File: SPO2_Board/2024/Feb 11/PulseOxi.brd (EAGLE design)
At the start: 70 x 70 mm, 45 parts, among them IC1 AFE4400RHAR

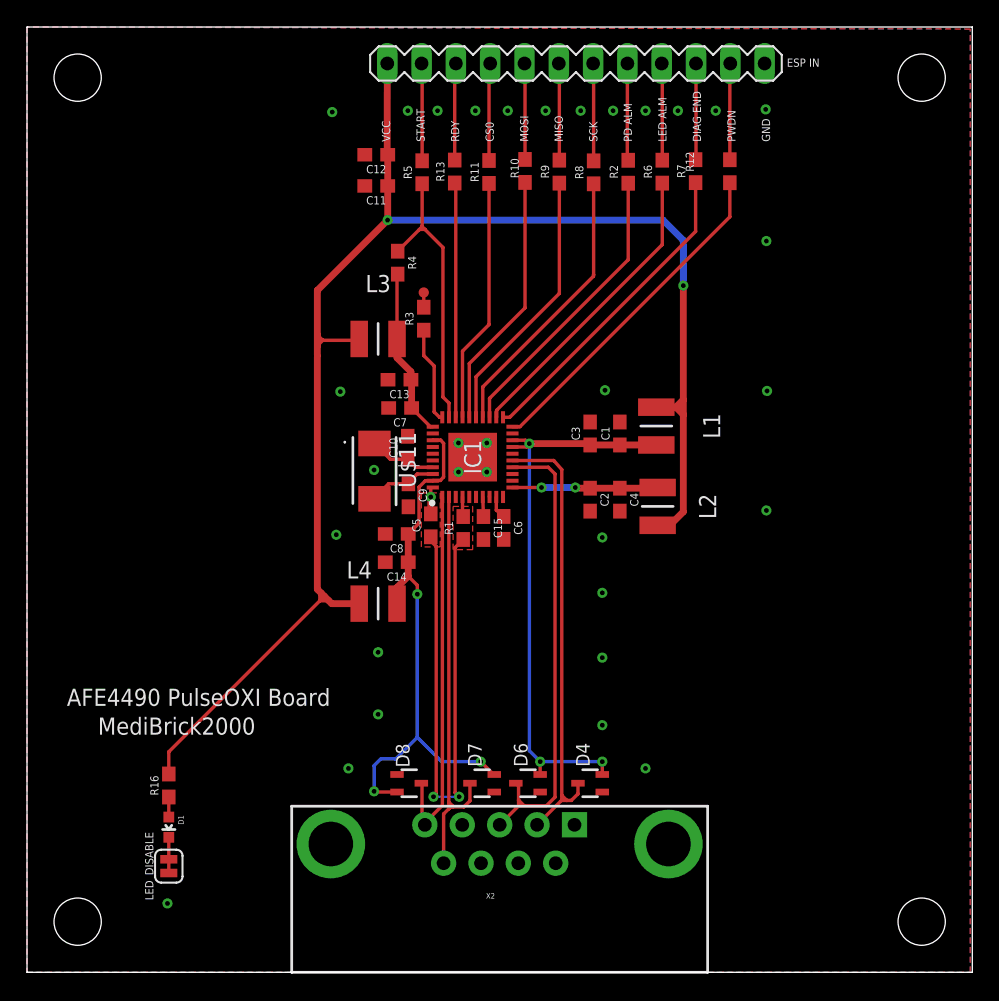
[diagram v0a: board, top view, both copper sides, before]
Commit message: Impedance
Minor change SPO2
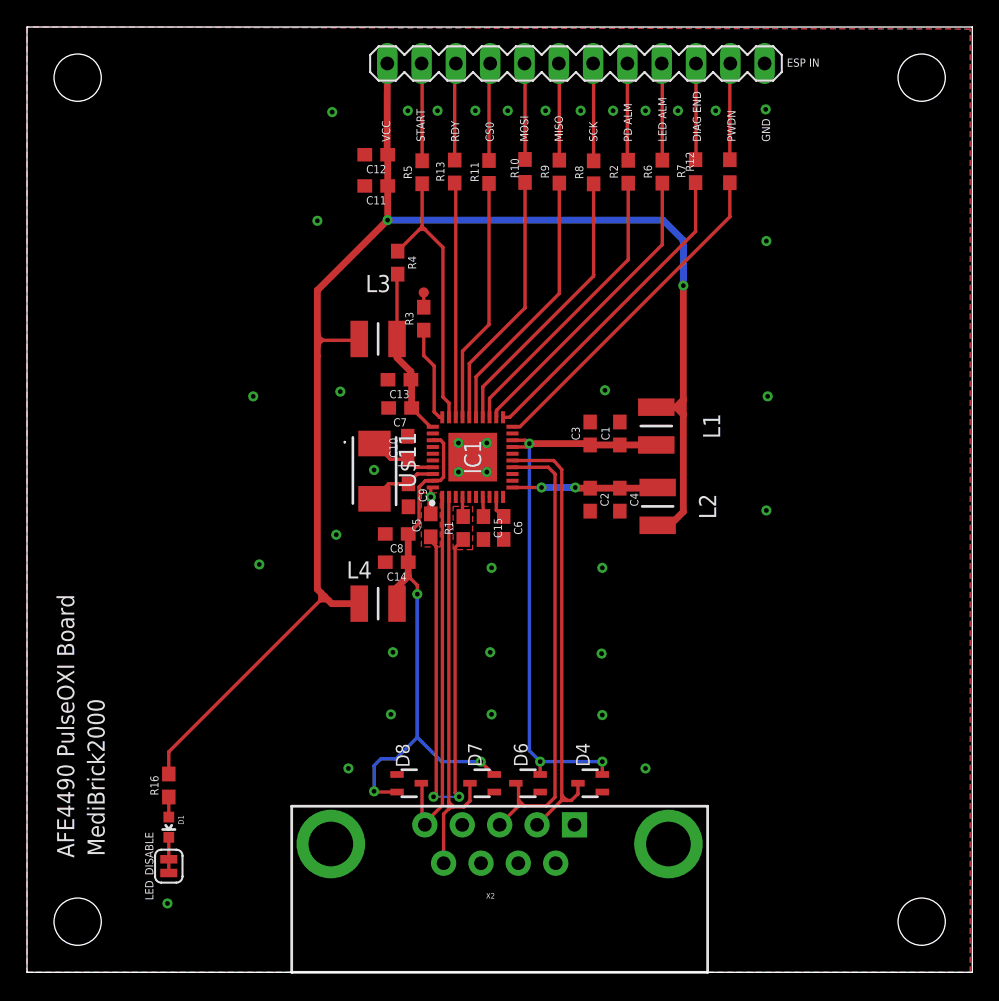
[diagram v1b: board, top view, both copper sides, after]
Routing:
- net GND: vias 33 -> 38
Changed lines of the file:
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@@
 <drawing>
 <settings>
-<setting alwaysvectorfont="no"/>
+<setting alwaysvectorfont="yes"/>
 <setting verticaltext="up"/>
 </settings>
@@
 <hole x="3.75" y="3.75" drill="3.5"/>
 <hole x="66.25" y="3.75" drill="3.5"/>
-<text x="5.250584375" y="17.598059375" size="1.27" layer="25">MediBrick2000</text>
-<text x="2.9499375" y="19.729053125" size="1.27" layer="25">AFE4490 PulseOXI Board</text>
+<text x="5.750584375" y="8.598059375" size="1.27" layer="25" rot="R90">MediBrick2000</text>
+<text x="3.4999375" y="8.479053125" size="1.27" layer="25" rot="R90">AFE4490 PulseOXI Board</text>
 <text x="55.023946875" y="61.5" size="0.6096" layer="25" rot="R90">GND</text>
 <text x="32.00608125" y="61.5" size="0.6096" layer="25" rot="R90">RDY</text>
@@
 <vertex x="29.2" y="31.5"/>
 </polygon>
-<via x="42.6" y="23.3" extent="1-16" drill="0.35"/>
-<via x="42.6" y="28.1" extent="1-16" drill="0.35"/>
-<via x="42.6" y="32.2" extent="1-16" drill="0.35"/>
+<via x="42.55" y="23.6" extent="1-16" drill="0.35"/>
+<via x="42.6" y="29.95" extent="1-16" drill="0.35"/>
 <via x="42.8" y="43.1" extent="1-16" drill="0.35"/>
-<via x="54.8" y="43.05" extent="1-16" drill="0.35"/>
+<via x="54.85" y="42.65" extent="1-16" drill="0.35"/>
 <via x="54.75" y="34.2" extent="1-16" drill="0.35"/>
 <via x="54.75" y="54.15" extent="1-16" drill="0.35"/>
@@
 <via x="28.2" y="63.8" extent="1-16" drill="0.35"/>
 <via x="22.6" y="63.7" extent="1-16" drill="0.35"/>
-<via x="42.6" y="18.3" extent="1-16" drill="0.35"/>
+<via x="42.6" y="19.05" extent="1-16" drill="0.35"/>
 <via x="45.8" y="15.1" extent="1-16" drill="0.35"/>
 <via x="23.8" y="15.1" extent="1-16" drill="0.35"/>
-<via x="26" y="19.1" extent="1-16" drill="0.35"/>
-<via x="26" y="23.7" extent="1-16" drill="0.35"/>
+<via x="26.95" y="19.1" extent="1-16" drill="0.35"/>
+<via x="27.1" y="23.7" extent="1-16" drill="0.35"/>
 <via x="10.4" y="5.1" extent="1-16" drill="0.35"/>
 <contactref element="C5" pad="2"/>
@@
 <wire x1="33" y1="38.15" x2="33" y2="38.1" width="0.1524" layer="1"/>
 <wire x1="33" y1="38.1" x2="34.05" y2="37.05" width="0.1524" layer="1"/>
+<via x="34.4" y="19.1" extent="1-16" drill="0.35"/>
+<via x="34.3" y="23.7" extent="1-16" drill="0.35"/>
+<via x="34.4" y="29.95" extent="1-16" drill="0.35"/>
+<via x="17.2" y="30.2" extent="1-16" drill="0.35"/>
+<via x="16.75" y="42.65" extent="1-16" drill="0.35"/>
+<via x="21.5" y="55.65" extent="1-16" drill="0.35"/>
 </signal>
 <signal name="PWDN">
